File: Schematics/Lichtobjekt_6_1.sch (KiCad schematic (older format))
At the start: 60 parts, among them IC1 STM32F10XCXT6, IC2 TSOP348, IC4 RV-3029-C2, IC6 24SN, J6 22-?-0427-2041, Q1 32,768 MS1V-7, Q2 12MHz, SW2 EC11B-V-T, T1 SFH320, T3 BSS138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

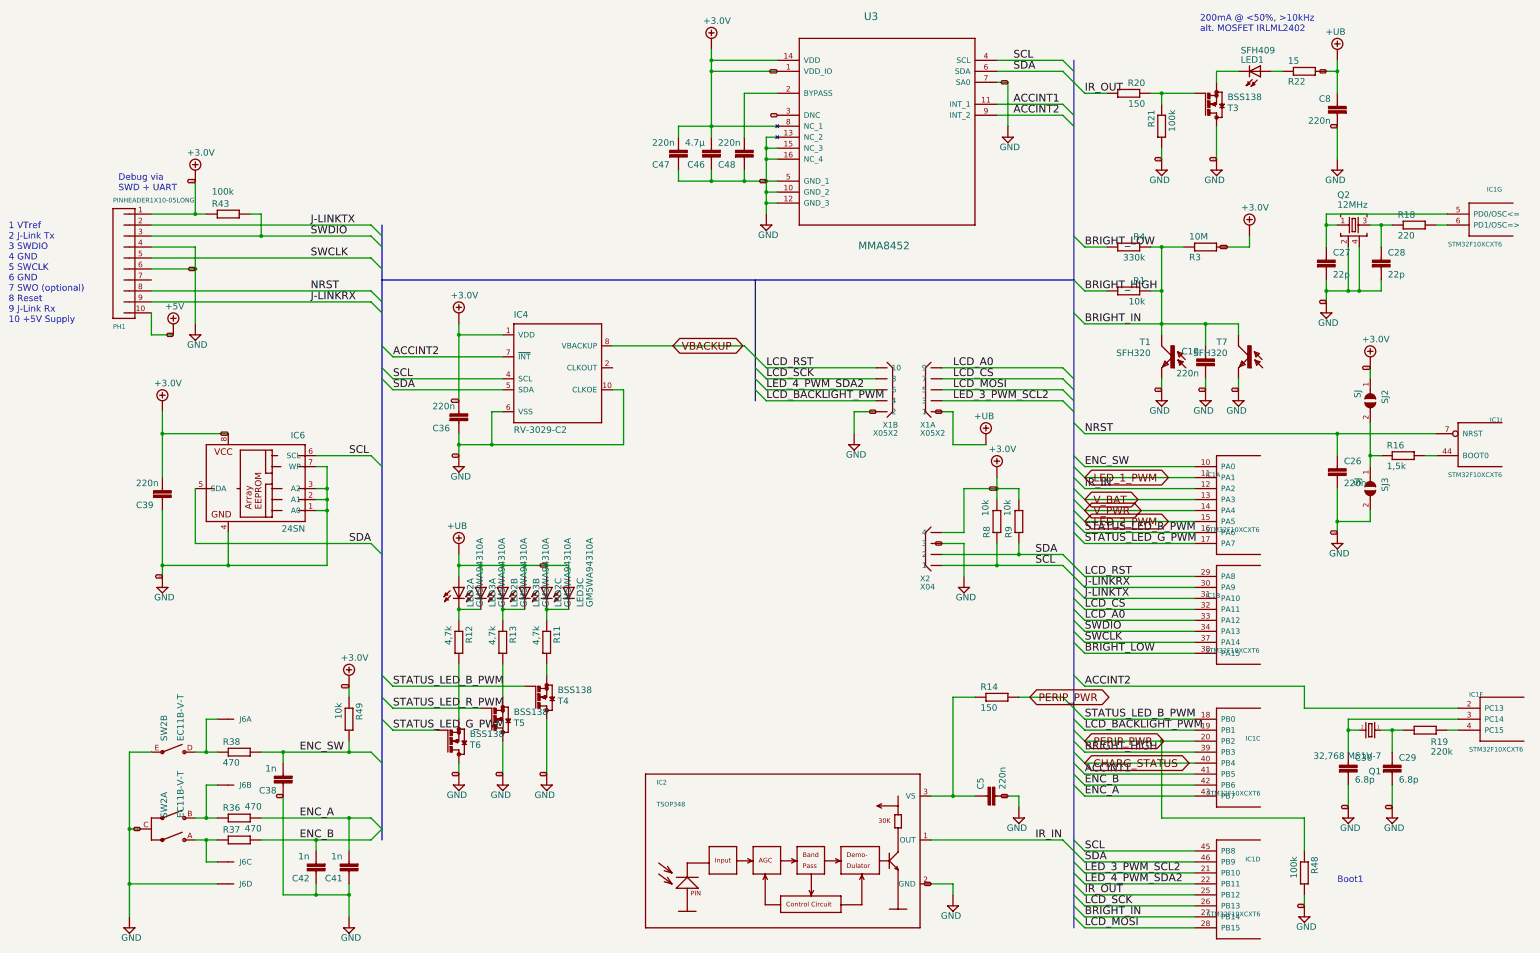
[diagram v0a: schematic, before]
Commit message: version of PCB produced first version to show basic functionality incl. remote and serial monitor output
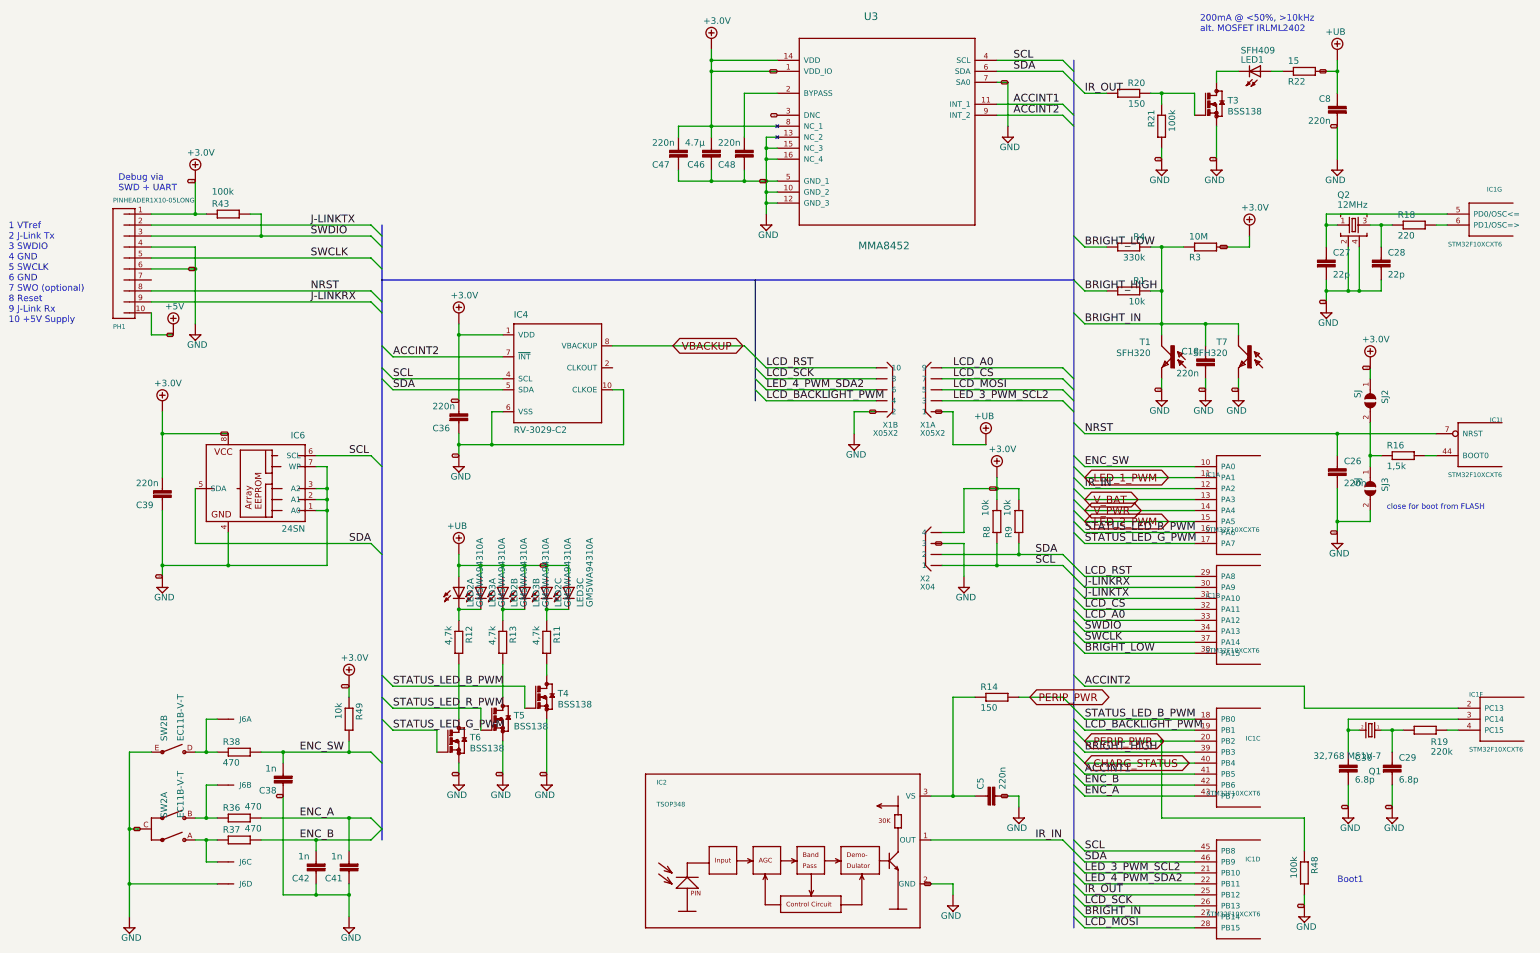
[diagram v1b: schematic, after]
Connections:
- net GND: now also T3.2 (S), T4.2 (S), T5.2 (S), T6.2 (S); no longer T3.3 (D), T4.3 (D), T5.3 (D), T6.3 (D)
- net at R13.2: now also T5.3 (D); no longer T5.2 (S)
- net at R11.2: now also T4.3 (D); no longer T4.2 (S)
- net at R12.2: now also T6.3 (D); no longer T6.2 (S)
- net at LED1.K (C): now also T3.3 (D); no longer T3.2 (S)
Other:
- note added: "close for boot from FLASH"
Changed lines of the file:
@@
 F 3 "" H 11700 1600 50  0001 C CNN
 	1    11700 1600
-	1    0    0    1
+	1    0    0    -1
 $EndComp
 $Comp
@@
 F 3 "" H 5600 7000 50  0001 C CNN
 	1    5600 7000
-	1    0    0    1
+	1    0    0    -1
 $EndComp
 $Comp
@@
 F 3 "" H 5200 7200 50  0001 C CNN
 	1    5200 7200
-	1    0    0    1
+	1    0    0    -1
 $EndComp
 $Comp
@@
 F 3 "" H 4800 7400 50  0001 C CNN
 	1    4800 7400
-	1    0    0    1
+	1    0    0    -1
 $EndComp
 $Comp
@@
 Text Label 10500 7200 0    70   ~ 0
 STATUS_LED_B_PWM
+Text Notes 13250 5300 0    50   ~ 0
+close for boot from FLASH
+Wire Wire Line
+	5400 6900 5400 7100
+Wire Wire Line
+	5000 7100 5000 7300
+Wire Wire Line
+	4600 7300 4600 7500
+Wire Wire Line
+	11500 1700 11500 1500
 Wire Bus Line
 	4100 2700 4100 3200
